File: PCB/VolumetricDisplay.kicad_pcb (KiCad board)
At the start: 4 copper layers, 48.5 x 56 mm, 201 parts, among them J1 USB_C_Receptacle_USB2.0_16P, Q1 MMFTN620KD, Q2 MMFTN620KD, Q3 MMFTN620KD, Q4 MMFTN620KD, U1 FT260S-R, U2 NCP718xSN330, U3 STM32G071R8T6, U4 DRV8311S, U5 DRV5055A1xDBZxQ1

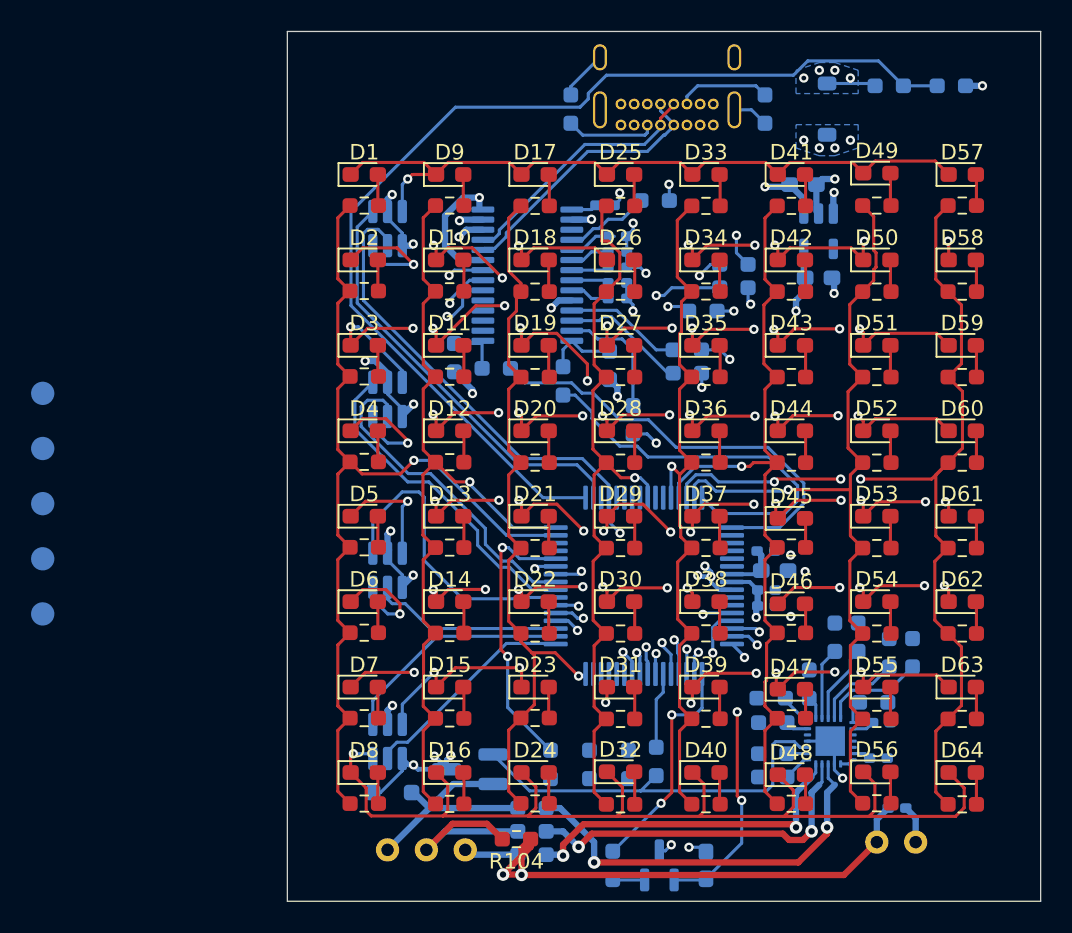
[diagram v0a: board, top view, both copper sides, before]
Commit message: Finished routing board, just need to double check last 255 warnings, fix BOM, and order.
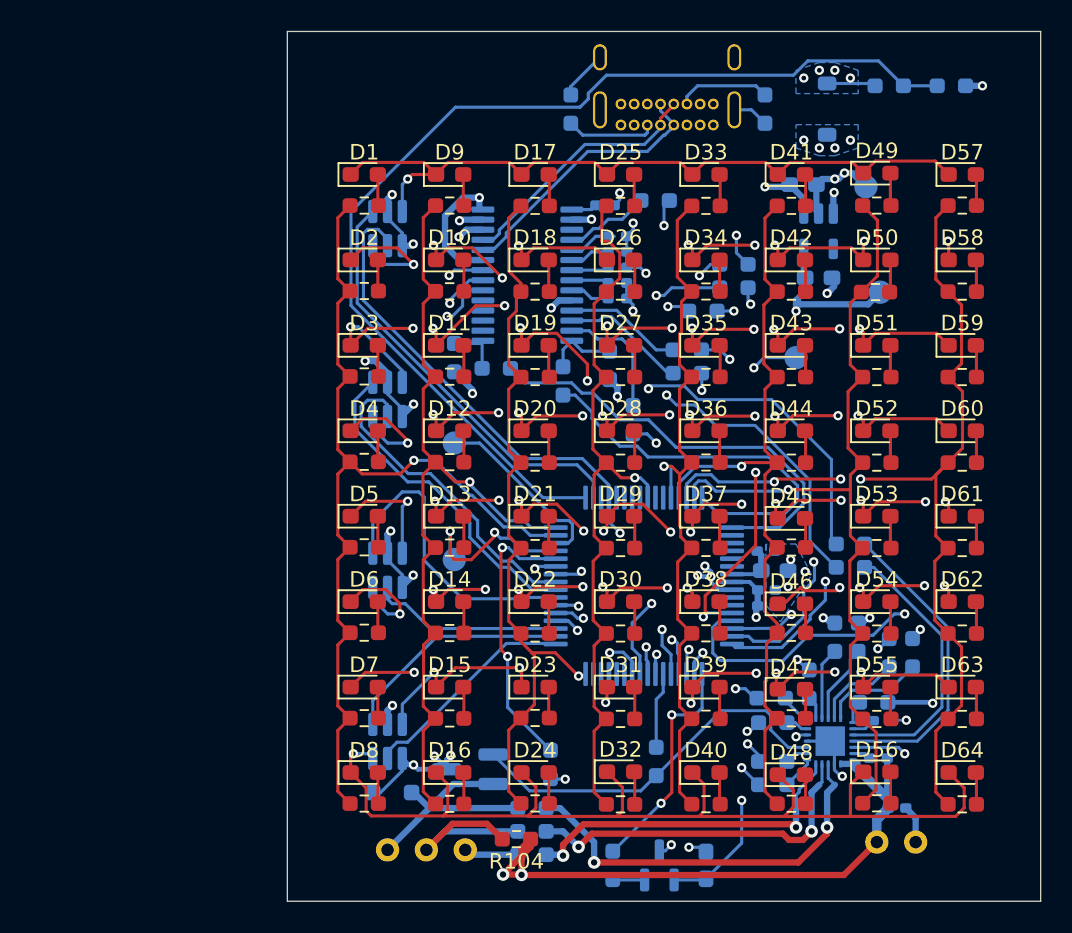
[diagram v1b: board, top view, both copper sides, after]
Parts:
- moved TP5 59.7 mm to (149.5, 85.0)
- moved 3V3 54.3 mm to (150.4, 91.8)
- moved nRST 50.2 mm to (145.0, 96.0)
- moved TP2 27.4 mm to (123.0, 109.0)
- moved TP3 26.8 mm to (123.0, 101.5)
- moved R85 22.0 mm to (148.5, 108.0), turned to 0 degrees
- moved R86 19.1 mm to (148.5, 109.5), turned to 0 degrees
- moved R80 0.50 mm to (143.5, 122.0)
- moved R82 0.50 mm to (143.5, 123.5)
- moved C1 0.13 mm to (150.5, 119.4)
- moved R50 0.09 mm to (150.1, 91.8)
- renumbered TP1 to 3V3, TP4 to nRST
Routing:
- net 3V3: track 24.9 -> 129.3 mm, vias 6 -> 5
- net Net-(U3-PA10/UCPD1_DBCC2): track 1.74 -> 36.5 mm, vias 1 -> 2
- net Net-(U3-PA9/UCPD1_DBCC1): track 1.92 -> 32.1 mm, vias 1 -> 2
- net Net-(U3-PD1): track 2.78 -> 32.2 mm, vias 1 -> 2
- net MTR_ISENA: track 0.00 -> 29.3 mm, vias 0 -> 2
- net Net-(U3-PC0): track 24.3 -> 53.0 mm
- net Net-(U3-PA9/PA11): track 1.41 -> 28.4 mm, vias 1 -> 2
- net nRST: track 1.90 -> 23.2 mm, vias 1 -> 3
- net MTR_ISENB: track 0.00 -> 19.9 mm
- net Net-(U3-PA4): track 2.25 -> 22.0 mm, vias 1 -> 2
- net MTR_ISENC: track 0.00 -> 17.9 mm
- net Net-(U3-PA8): track 1.68 -> 16.7 mm, vias 1 -> 2
- net Net-(U3-PA2): track 1.61 -> 15.2 mm, vias 1 -> 2
- net Net-(U3-PC2): track 17.4 -> 30.9 mm
- net Net-(U3-PC3): track 22.8 -> 35.6 mm
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- added copper zone on B.Cu, net GND

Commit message: Made various changes for increased readability
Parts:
- added G***: LOGO, logos:IEEE, B.Cu at (153.3, 95.6)
- added G***: LOGO, logos:BYU, B.Cu at (152.5, 100.6)
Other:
- board text added: "Student Branch Jul 2026"

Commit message: Generated release package X0
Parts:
- added FID1: Fiducial, Fiducial:Fiducial_0.5mm_Mask1mm, F.Cu at (159.5, 76.5)
- added FID2: Fiducial, Fiducial:Fiducial_0.5mm_Mask1mm, F.Cu at (113.5, 129.5)
- added FID3: Fiducial, Fiducial:Fiducial_0.5mm_Mask1mm, B.Cu at (113.5, 76.5)
- added FID4: Fiducial, Fiducial:Fiducial_0.5mm_Mask1mm, B.Cu at (159.5, 129.5)
- renumbered 3V3 to TP1, nRST to TP4
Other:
- board text added: "REV X0"
- board text added: "Volumetric Display"

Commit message: Fixed Q1-Q4, re-released
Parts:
- Q1, Q2, Q3, Q4: value MMFTN620KD -> DMN32D2LDF; footprint Package_TO_SOT_SMD:SOT-457T -> Package_TO_SOT_SMD:SOT-353_SC-70-5
- moved Q1 0.77 mm to (118.0, 88.0), turned to 0 degrees
- moved Q2 0.77 mm to (118.0, 99.0), turned to 0 degrees
- moved Q3 0.77 mm to (118.0, 110.0), turned to 0 degrees
- moved Q4 0.17 mm to (118.6, 120.5)
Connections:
- Q1 pad 1: LED8 -> LED9
- Q1 pad 3: FET0 -> LED8
- Q1 pad 4: GND -> FET0
- Q1 pad 5: LED9 -> FET1
- Q2 pad 1: LED10 -> LED11
- Q2 pad 3: FET2 -> LED10
- Q2 pad 4: GND -> FET2
- Q2 pad 5: LED11 -> FET3
- Q3 pad 1: LED12 -> LED13
- Q3 pad 3: FET4 -> LED12
- Q3 pad 4: GND -> FET4
- Q3 pad 5: LED13 -> FET5
- Q4 pad 3: FET6 -> LED15
- Q4 pad 4: GND -> FET6
- Q4 pad 5: LED15 -> FET7
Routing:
- net GND: track 64.8 -> 57.9 mm
- net LED11: track 21.3 -> 17.8 mm
- net LED9: track 28.2 -> 25.2 mm
- net FET6: track 52.1 -> 54.0 mm
- net LED13: track 12.4 -> 13.7 mm
- net FET1: track 59.0 -> 57.6 mm
- net USB_DET: track 68.9 -> 70.0 mm
- net FET4: track 52.4 -> 53.5 mm
- net FET0: track 47.2 -> 48.3 mm
- net FET3: track 51.9 -> 50.8 mm
- net LED12: track 19.9 -> 20.9 mm
- net FET5: track 56.3 -> 55.5 mm
- net LED15: track 14.2 -> 13.6 mm
